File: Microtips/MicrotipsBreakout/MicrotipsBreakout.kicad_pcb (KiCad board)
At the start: 2 copper layers, 88.6 x 56.3 mm, 16 parts, among them J1 Conn_01x24_Pin, Q1 Si1308EDL

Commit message: update
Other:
- board size 88.6 x 56.3 mm -> 100.7 x 66.2 mm
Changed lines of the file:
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@@
 		(tags "SOT-323 SC-70")
 		(property "Reference" "Q1"
-			(at -0.05 -2.25 360)
+			(at -0.05 -2.25 0)
 			(layer "F.SilkS")
 			(effects
@@
 		)
 		(property "Value" "Si1308EDL"
-			(at -0.05 2.05 360)
+			(at -0.05 2.05 0)
 			(layer "F.Fab")
 			(hide yes)
@@
 		(tags "SOD-123")
 		(property "Reference" "D3"
-			(at 0.0925 1.6925 360)
+			(at 0.0925 1.6925 0)
 			(layer "F.SilkS")
 			(effects
@@
 		)
 		(property "Value" "MBR0530"
-			(at 0 2.1 360)
+			(at 0 2.1 0)
 			(layer "F.Fab")
 			(hide yes)
@@
 		(tags "SOD-123")
 		(property "Reference" "D2"
-			(at -0.0425 1.885 360)
+			(at -0.0425 1.885 0)
 			(layer "F.SilkS")
 			(effects
@@
 		)
 		(property "Value" "MBR0530"
-			(at 0 2.1 360)
+			(at 0 2.1 0)
 			(layer "F.Fab")
 			(hide yes)
@@
 			(at 0 5.4 0)
 			(layer "F.Fab")
-			(hide yes)
 			(effects
 				(font
@@
 			)
 		)
+		(model "${KIPRJMOD}/FPC-24.stp"
+			(offset
+				(xyz -5.75 2.1 0)
+			)
+			(scale
+				(xyz 1 1 1)
+			)
+			(rotate
+				(xyz 0 0 0)
+			)
+		)
 	)
 	(footprint "Capacitor_SMD:C_1206_3216Metric"
@@
 		(tags "SOD-123")
 		(property "Reference" "D1"
-			(at 0 -2 360)
+			(at 0 -2 0)
 			(layer "F.SilkS")
 			(effects
@@
 		)
 		(property "Value" "MBR0530"
-			(at 0 2.1 360)
+			(at 0 2.1 0)
 			(layer "F.Fab")
 			(hide yes)
@@
 		)
 		(fp_text user "${REFERENCE}"
-			(at 0 -2 360)
+			(at 0 -2 0)
 			(layer "F.Fab")
 			(effects
@@
 			)
 		)
+		(model "${KIPRJMOD}/vls6045ex-h.step"
+			(offset
+				(xyz 0 0 2.3)
+			)
+			(scale
+				(xyz 1 1 1)
+			)
+			(rotate
+				(xyz -90 0 0)
+			)
+		)
 	)
 	(footprint "Capacitor_SMD:C_1206_3216Metric"
@@
 		)
 	)
-	(gr_line
-		(start 185.285 116.7675)
-		(end 96.695 116.7675)
-		(stroke
-			(width 0.05)
-			(type default)
-		)
-		(layer "Edge.Cuts")
-	)
-	(gr_line
-		(start 96.695 116.7675)
-		(end 96.695 60.4725)
-		(stroke
-			(width 0.05)
-			(type default)
-		)
-		(layer "Edge.Cuts")
-	)
-	(gr_line
-		(start 96.695 60.4725)
-		(end 97.32 60.4775)
-		(stroke
-			(width 0.05)
-			(type default)
-		)
-		(layer "Edge.Cuts")
-	)
-	(gr_line
-		(start 185.0775 60.58)
-		(end 185.285 116.7675)
-		(stroke
-			(width 0.05)
-			(type default)
-		)
-		(layer "Edge.Cuts")
-	)
-	(gr_line
-		(start 97.32 60.4775)
-		(end 185.0775 60.58)
+	(gr_rect
+		(start 90.22 55.1675)
+		(end 190.905 121.32)
 		(stroke
 			(width 0.05)
 			(type default)
 		)
+		(fill none)
 		(layer "Edge.Cuts")
 	)

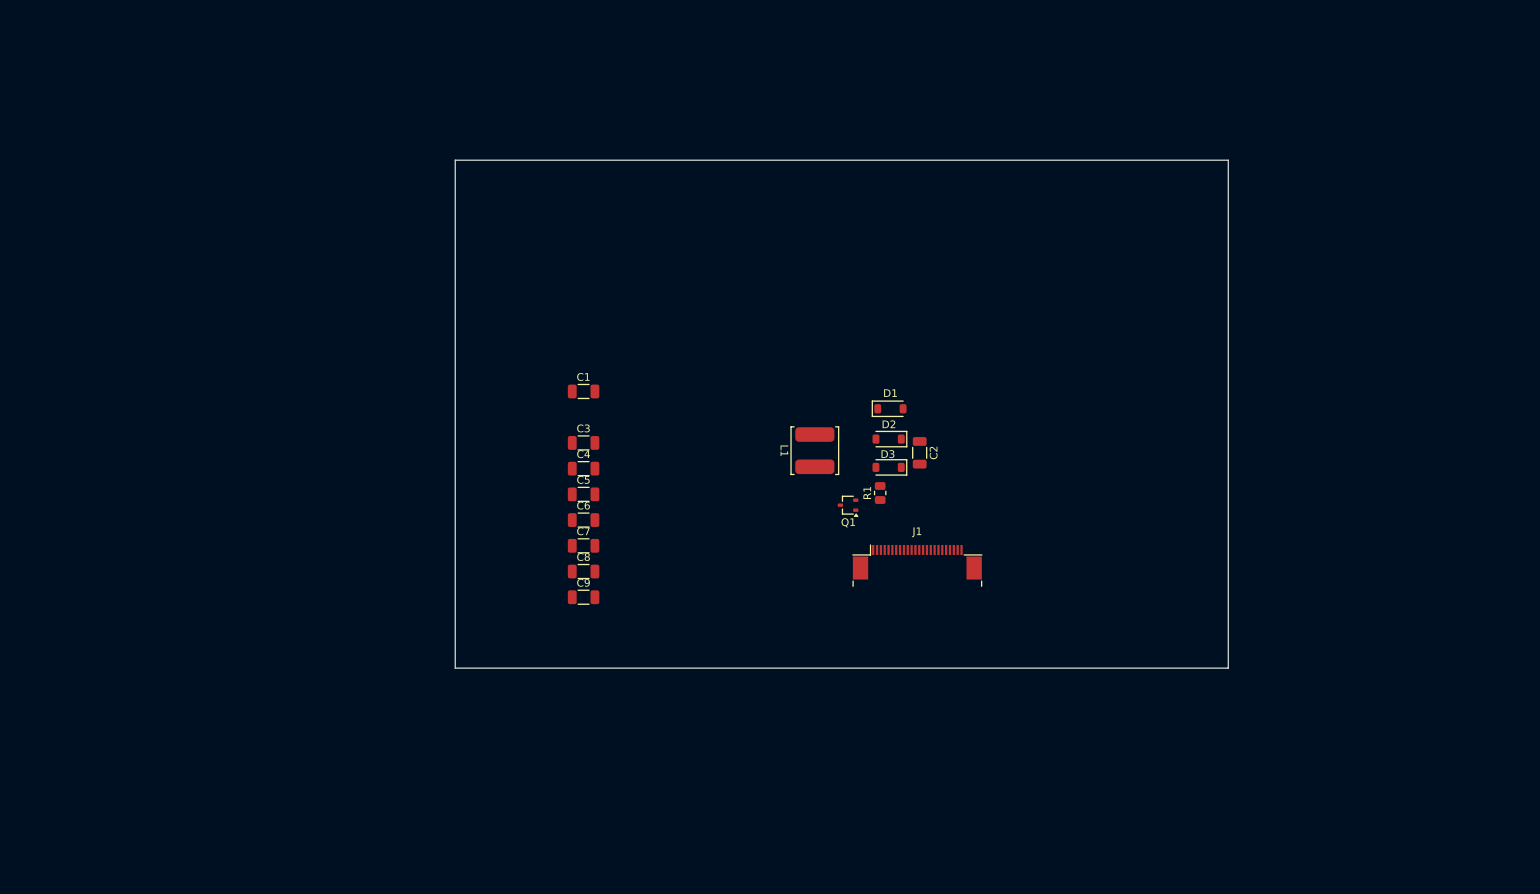
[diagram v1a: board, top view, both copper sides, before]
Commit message: Added Pico
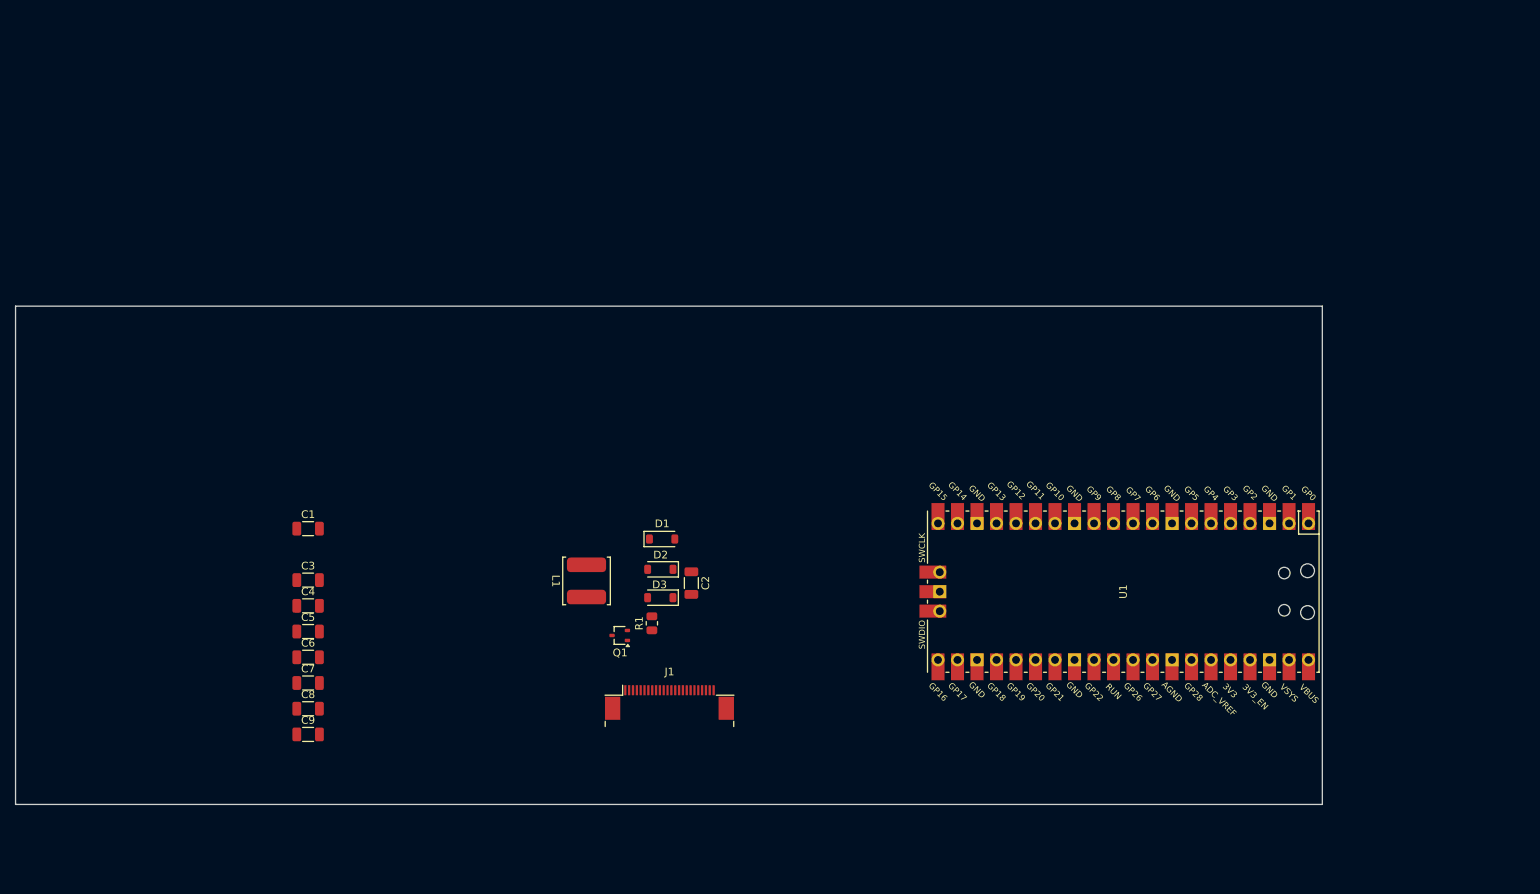
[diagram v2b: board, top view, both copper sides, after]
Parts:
- added U1: Pico, MCU_RaspberryPi_and_Boards:RPi_Pico_SMD_TH, F.Cu at (177.2, 111.4)
- moved C1 40.1 mm to (71.1, 103.2)
- moved C3 40.1 mm to (71.1, 109.9)
- moved C5 40.1 mm to (71.1, 116.6)
- moved C6 40.1 mm to (71.1, 119.9)
- moved C8 40.1 mm to (71.1, 126.6)
- moved C9 40.1 mm to (71.1, 130.0)
- moved C4 40.1 mm to (71.1, 113.2)
- moved C7 40.1 mm to (71.1, 123.3)
- moved J1 37.1 mm to (118.1, 125.8)
- moved C2 34.2 mm to (121.0, 110.2)
- moved D1 34.2 mm to (117.2, 104.5)
- moved L1 34.2 mm to (107.3, 110.0)
- moved D2 34.2 mm to (116.9, 108.5)
- moved D3 34.2 mm to (116.9, 112.1)
- moved Q1 34.2 mm to (111.6, 117.1)
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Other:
- board size 100.7 x 66.2 mm -> 170.2 x 64.9 mm

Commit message: made graphics; building EPD driver
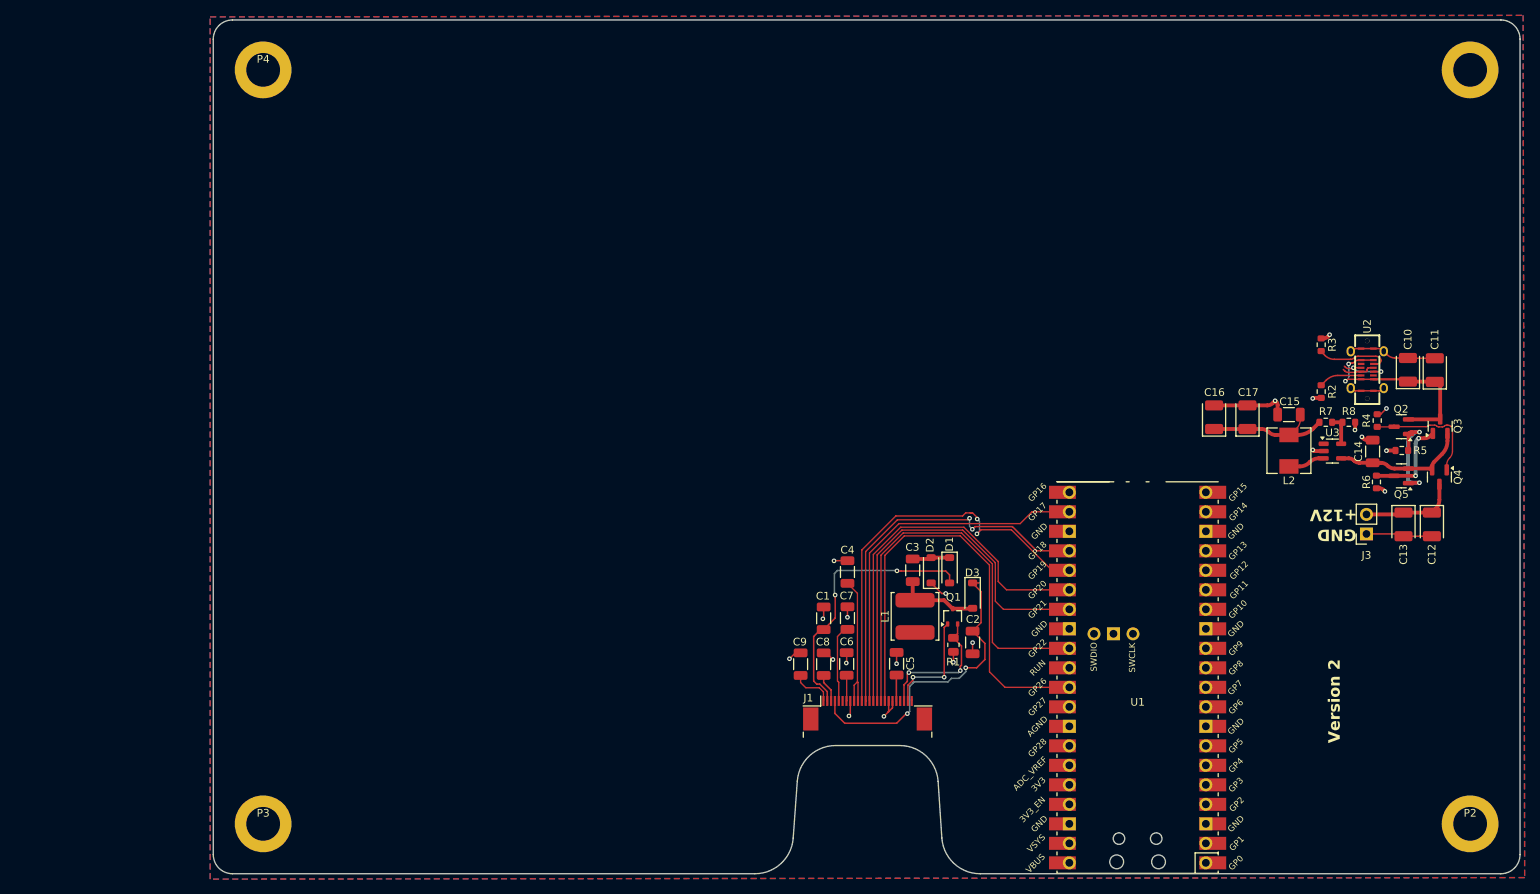
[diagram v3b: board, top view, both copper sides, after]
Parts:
- added C10: 10uF, Capacitor_Tantalum_SMD:CP_EIA-3528-12_Kemet-T, F.Cu at (214.3, 82.5)
- added C11: 10uF, Capacitor_Tantalum_SMD:CP_EIA-3528-12_Kemet-T, F.Cu at (217.8, 82.5)
- added C12: 10uF, Capacitor_Tantalum_SMD:CP_EIA-3528-12_Kemet-T, F.Cu at (217.4, 102.6)
- added C13: 10uF, Capacitor_Tantalum_SMD:CP_EIA-3528-12_Kemet-T, F.Cu at (213.7, 102.6)
- added C14: 10uF, Capacitor_SMD:C_1206_3216Metric, F.Cu at (209.7, 93.1)
- added C15: 10uF, Capacitor_SMD:C_1206_3216Metric, F.Cu at (198.8, 88.3)
- added C16: 10uF, Capacitor_Tantalum_SMD:CP_EIA-3528-12_Kemet-T, F.Cu at (189.1, 88.6)
- added C17: 10uF, Capacitor_Tantalum_SMD:CP_EIA-3528-12_Kemet-T, F.Cu at (193.4, 88.6)
- added J3: Conn_01x02_Socket, Connector_PinSocket_2.54mm:PinSocket_1x02_P2.54mm_Vertical, F.Cu at (208.9, 103.8)
- added L2: L, Inductor_SMD:L_Chilisin_BMRB00050518-B, F.Cu at (198.8, 93.0)
- added P1: ~, WuerthMounting:9774060360R, F.Cu at (222.4, 43.4)
- added P2: ~, WuerthMounting:9774060360R, F.Cu at (222.4, 141.6)
- added P3: ~, WuerthMounting:9774060360R, F.Cu at (65.2, 141.6)
- added P4: ~, WuerthMounting:9774060360R, F.Cu at (65.2, 43.4)
- added Q2: PNP, Package_TO_SOT_SMD:SOT-23, F.Cu at (213.4, 89.9)
- added Q3: PMOS, Package_TO_SOT_SMD:SOT-23, F.Cu at (218.5, 89.8)
- added Q4: PMOS, Package_TO_SOT_SMD:SOT-23, F.Cu at (218.4, 96.4)
- added Q5: PNP, Package_TO_SOT_SMD:SOT-23, F.Cu at (213.4, 96.3)
- added R2: 5.1k, Resistor_SMD:R_0603_1608Metric, F.Cu at (203.0, 85.3)
- added R3: 5.1k, Resistor_SMD:R_0603_1608Metric, F.Cu at (203.0, 79.2)
- added R4: 100k, Resistor_SMD:R_0603_1608Metric, F.Cu at (210.3, 89.1)
- added R5: 100k, Resistor_SMD:R_0603_1608Metric, F.Cu at (213.5, 93.0)
- added R6: 100k, Resistor_SMD:R_0603_1608Metric, F.Cu at (210.2, 97.1)
- added R7: 61.9k, Resistor_SMD:R_0603_1608Metric, F.Cu at (203.6, 89.3)
- added R8: 20k, Resistor_SMD:R_0603_1608Metric, F.Cu at (206.6, 89.3)
- added U2: TYPE-C 16PLT-H10.0, EasyEDA:TYPE-C-SMD_USB4120-03-C, F.Cu at (209.0, 82.5)
- added U3: TPS560200, Package_TO_SOT_SMD:SOT-23-5, F.Cu at (204.5, 93.0)
- moved C3 78.8 mm to (149.8, 108.6), turned to -90 degrees
- moved C5 76.8 mm to (147.7, 120.8), turned to 90 degrees
- moved C7 70.8 mm to (141.3, 114.8), turned to 90 degrees
- moved C4 70.4 mm to (141.3, 108.8), turned to 90 degrees
- moved C6 70.2 mm to (141.2, 120.8), turned to 90 degrees
- moved C1 68.2 mm to (138.2, 114.8), turned to 90 degrees
- moved C8 67.4 mm to (138.2, 120.8), turned to 90 degrees
- moved C9 64.8 mm to (135.2, 120.8), turned to 90 degrees
- moved Q1 43.4 mm to (155.0, 114.6), turned to 90 degrees
- moved L1 43.0 mm to (150.1, 114.6), turned to 90 degrees
- moved D3 40.7 mm to (157.6, 111.9), turned to -90 degrees
- moved R1 39.4 mm to (155.1, 118.3), turned to -90 degrees
- moved D1 37.7 mm to (154.6, 108.6), turned to -90 degrees
- moved C2 37.4 mm to (157.6, 118.0), turned to 90 degrees
- moved D2 35.3 mm to (152.2, 108.6), turned to 90 degrees
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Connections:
- C4 pad 1: VCI -> 3V3
- C5 pad 1: Net-(J1-Pin_5) -> Net-(J1-Pin_20)
- C6 pad 1: Net-(J1-Pin_18) -> Net-(J1-Pin_7)
- C7 pad 1: Net-(J1-Pin_20) -> Net-(J1-Pin_5)
- C8 pad 1: Net-(J1-Pin_22) -> Net-(J1-Pin_3)
- C9 pad 1: Net-(J1-Pin_24) -> Net-(J1-Pin_1)
- J1 pad 1: unconnected-(J1-Pin_1-Pad1) -> Net-(J1-Pin_1)
- J1 pad 10: RES# -> 3V3
- J1 pad 11: D/C# -> SDA
- J1 pad 12: CS# -> SCL
- J1 pad 13: SCL -> CS#
- J1 pad 14: SDA -> D/C#
- J1 pad 15: VCI -> RES#
- J1 pad 16: VCI -> BUSY
- J1 pad 17: GND -> BS
- J1 pad 18: Net-(J1-Pin_18) -> GND
- J1 pad 19: unconnected-(J1-Pin_19-Pad19) -> GND
- J1 pad 2: GDR -> VGL
- J1 pad 21: VGH -> unconnected-(J1-Pin_21-Pad21)
- J1 pad 22: Net-(J1-Pin_22) -> RESE
- J1 pad 23: VGL -> GDR
- J1 pad 24: Net-(J1-Pin_24) -> unconnected-(J1-Pin_24-Pad24)
- J1 pad 3: RESE -> Net-(J1-Pin_3)
- J1 pad 4: unconnected-(J1-Pin_4-Pad4) -> VGH
- J1 pad 6: TSCL -> unconnected-(J1-Pin_6-Pad6)
- J1 pad 7: TSDA -> Net-(J1-Pin_7)
- J1 pad 8: BS -> GND
- J1 pad 9: BUSY -> 3V3
- L1 pad 1: VCI -> 3V3
- U1 pad 13: unconnected-(U1-GND-Pad13) -> GND
- U1 pad 18: unconnected-(U1-GND-Pad18) -> GND
- U1 pad 22: unconnected-(U1-GPIO17-Pad22) -> CS#
- U1 pad 23: unconnected-(U1-GND-Pad23) -> GND
- U1 pad 24: unconnected-(U1-GPIO18-Pad24) -> SCL
- U1 pad 25: unconnected-(U1-GPIO19-Pad25) -> SDA
- U1 pad 26: unconnected-(U1-GPIO20-Pad26) -> D/C#
- U1 pad 27: unconnected-(U1-GPIO21-Pad27) -> RES#
- U1 pad 28: unconnected-(U1-GND-Pad28) -> GND
- U1 pad 29: unconnected-(U1-GPIO22-Pad29) -> BUSY
- U1 pad 3: unconnected-(U1-GND-Pad3) -> GND
- U1 pad 31: unconnected-(U1-GPIO26_ADC0-Pad31) -> BS
- U1 pad 38: unconnected-(U1-GND-Pad38) -> GND
- U1 pad 39: unconnected-(U1-VSYS-Pad39) -> 3V3
- U1 pad 42: unconnected-(U1-GND-Pad42) -> GND
- U1 pad 8: unconnected-(U1-GND-Pad8) -> GND
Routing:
- net GND: track 0.00 -> 67.9 mm, vias 0 -> 21
- net BS: track 0.00 -> 60.4 mm
- net BUSY: track 0.00 -> 57.4 mm
- net SDA: track 0.00 -> 54.0 mm, vias 0 -> 2
- net RES#: track 0.00 -> 53.1 mm
- net D/C#: track 0.00 -> 51.0 mm
- net SCL: track 0.00 -> 50.6 mm, vias 0 -> 2
- net CS#: track 0.00 -> 50.0 mm
- net VGH: track 0.00 -> 40.0 mm, vias 0 -> 2
- net 3V3: track 0.00 -> 38.6 mm
- net VGL: track 0.00 -> 35.5 mm, vias 0 -> 2
- net V_USB: track 0.00 -> 27.9 mm, vias 0 -> 2
- net RESE: track 0.00 -> 17.6 mm, vias 0 -> 2
- net VIN: track 0.00 -> 17.5 mm
- net Net-(Q2-C): track 0.00 -> 15.8 mm
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- added copper zone on F.Cu, net 3V3
- added copper zone on B.Cu, net GND
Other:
- board size 170.2 x 64.9 mm -> 170.2 x 111.2 mm
- board text added: "+12V"
- board text added: "GND"
- board text added: "Version 2"
